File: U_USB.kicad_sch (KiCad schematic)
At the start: 15 parts, among them J1 USB4085-GF-A_REVA, U8 ADUM4160

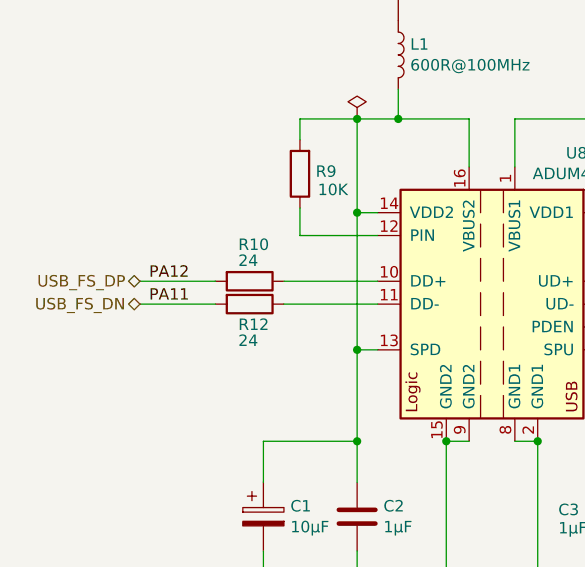
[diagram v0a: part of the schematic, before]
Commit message: KiCAD6.0 scheema rules check done
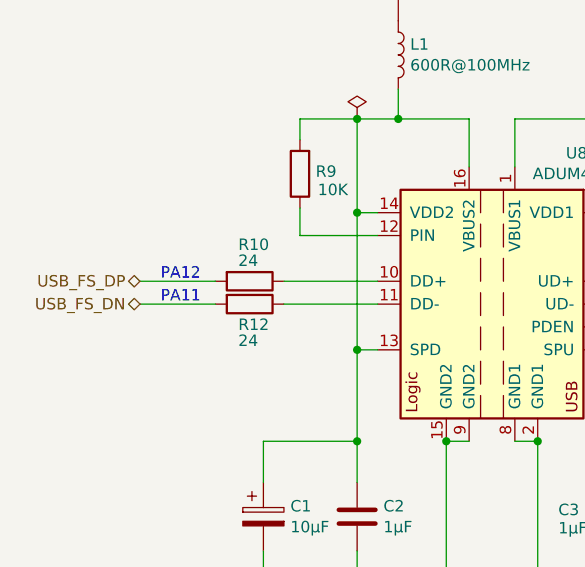
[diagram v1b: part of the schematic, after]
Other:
- note added: "PA11"
- note added: "PA12"
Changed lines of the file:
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@@
     (stroke (width 0) (type default) (color 0 0 0 0))
+  )
+  (text "PA11" (at 68.58 100.33 0)
+    (effects (font (size 1.27 1.27)) (justify left bottom))
+  )
+  (text "PA12" (at 68.58 97.79 0)
+    (effects (font (size 1.27 1.27)) (justify left bottom))
   )
   (text "ESD protection should\nbe near connector\n" (at 130.302 148.844 0)
@@
     (effects (font (size 1.27 1.27)) (justify left bottom))
   )
-  (label "PA11" (at 67.31 100.33 0)
-    (effects (font (size 1.27 1.27)) (justify left bottom))
-  )
   (label "USB_GND" (at 164.846 138.684 0)
     (effects (font (size 1.27 1.27)) (justify left bottom))
   )
-  (label "PA12" (at 67.31 97.79 0)
-    (effects (font (size 1.27 1.27)) (justify left bottom))
-  )

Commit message: All handsolder footprints removed
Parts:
- C2, C3, C4: footprint Capacitor_SMD:C_0603_1608Metric_Pad1.08x0.95mm_HandSolder -> Capacitor_SMD:C_0603_1608Metric
- L1: footprint Inductor_SMD:L_0805_2012Metric_Pad1.15x1.40mm_HandSolder -> Inductor_SMD:L_0805_2012Metric
- R10, R11, R12, R13, R14, R15, R9: footprint Resistor_SMD:R_0805_2012Metric_Pad1.20x1.40mm_HandSolder -> Resistor_SMD:R_0805_2012Metric
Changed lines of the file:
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@@
       (effects (font (size 1.27 1.27)) (justify left))
     )
-    (property "Footprint" "Resistor_SMD:R_0805_2012Metric_Pad1.20x1.40mm_HandSolder" (id 2) (at 85.852 85.852 90)
+    (property "Footprint" "Resistor_SMD:R_0805_2012Metric" (id 2) (at 85.852 85.852 90)
       (effects (font (size 1.27 1.27)) hide)
     )
@@
       (effects (font (size 1.27 1.27)) (justify left))
     )
-    (property "Footprint" "Resistor_SMD:R_0805_2012Metric_Pad1.20x1.40mm_HandSolder" (id 2) (at 153.924 128.016 90)
+    (property "Footprint" "Resistor_SMD:R_0805_2012Metric" (id 2) (at 153.924 128.016 90)
       (effects (font (size 1.27 1.27)) hide)
     )
@@
       (effects (font (size 1.27 1.27)) (justify left))
     )
-    (property "Footprint" "Resistor_SMD:R_0805_2012Metric_Pad1.20x1.40mm_HandSolder" (id 2) (at 161.29 128.016 90)
+    (property "Footprint" "Resistor_SMD:R_0805_2012Metric" (id 2) (at 161.29 128.016 90)
       (effects (font (size 1.27 1.27)) hide)
     )
@@
       (effects (font (size 1.27 1.27)) (justify left))
     )
-    (property "Footprint" "Resistor_SMD:R_0805_2012Metric_Pad1.20x1.40mm_HandSolder" (id 2) (at 125.222 96.012 90)
+    (property "Footprint" "Resistor_SMD:R_0805_2012Metric" (id 2) (at 125.222 96.012 90)
       (effects (font (size 1.27 1.27)) hide)
     )
@@
       (effects (font (size 1.27 1.27)) (justify left))
     )
-    (property "Footprint" "Resistor_SMD:R_0805_2012Metric_Pad1.20x1.40mm_HandSolder" (id 2) (at 125.222 98.552 90)
+    (property "Footprint" "Resistor_SMD:R_0805_2012Metric" (id 2) (at 125.222 98.552 90)
       (effects (font (size 1.27 1.27)) hide)
     )
@@
       (effects (font (size 1.27 1.27)) (justify left))
     )
-    (property "Footprint" "Capacitor_SMD:C_0603_1608Metric_Pad1.08x0.95mm_HandSolder" (id 2) (at 131.7752 127.762 0)
+    (property "Footprint" "Capacitor_SMD:C_0603_1608Metric" (id 2) (at 131.7752 127.762 0)
       (effects (font (size 1.27 1.27)) hide)
     )
@@
       (effects (font (size 1.27 1.27)) (justify left))
     )
-    (property "Footprint" "Capacitor_SMD:C_0603_1608Metric_Pad1.08x0.95mm_HandSolder" (id 2) (at 120.8532 127.762 0)
+    (property "Footprint" "Capacitor_SMD:C_0603_1608Metric" (id 2) (at 120.8532 127.762 0)
       (effects (font (size 1.27 1.27)) hide)
     )
@@
       (effects (font (size 1.27 1.27)) (justify left))
     )
-    (property "Footprint" "Capacitor_SMD:C_0603_1608Metric_Pad1.08x0.95mm_HandSolder" (id 2) (at 91.3892 127.762 0)
+    (property "Footprint" "Capacitor_SMD:C_0603_1608Metric" (id 2) (at 91.3892 127.762 0)
       (effects (font (size 1.27 1.27)) hide)
     )
@@
       (effects (font (size 1.27 1.27)) (justify left))
     )
-    (property "Footprint" "Inductor_SMD:L_0805_2012Metric_Pad1.15x1.40mm_HandSolder" (id 2) (at 94.996 72.644 0)
+    (property "Footprint" "Inductor_SMD:L_0805_2012Metric" (id 2) (at 94.996 72.644 0)
       (effects (font (size 1.27 1.27)) hide)
     )
@@
       (effects (font (size 1.27 1.27)) (justify left))
     )
-    (property "Footprint" "Resistor_SMD:R_0805_2012Metric_Pad1.20x1.40mm_HandSolder" (id 2) (at 78.486 96.012 90)
+    (property "Footprint" "Resistor_SMD:R_0805_2012Metric" (id 2) (at 78.486 96.012 90)
       (effects (font (size 1.27 1.27)) hide)
     )
@@
       (effects (font (size 1.27 1.27)) (justify left))
     )
-    (property "Footprint" "Resistor_SMD:R_0805_2012Metric_Pad1.20x1.40mm_HandSolder" (id 2) (at 78.486 98.552 90)
-      (effects (font (size 1.27 1.27)) hide)
-    )
+    (property "Footprint" "Resistor_SMD:R_0805_2012Metric" (id 2) (at 78.486 98.552 90)
+      (effects (font (size 1.27 1.27)) hide)
+    )
